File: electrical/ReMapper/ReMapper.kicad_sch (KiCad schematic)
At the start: 50 parts, among them J1 ESP_UART0, J2 I2C Display, J3 USB_IN, J4 USB_OUT, J5 Programming Mode SW, U1 SPX1117M3-L-3-3/TR, U2 W25Q128JVE, U3 ESP32-S3-WROOM-1-N8R8, U4 RP2040, U5 W25Q128JVE, Y1 12MHZ

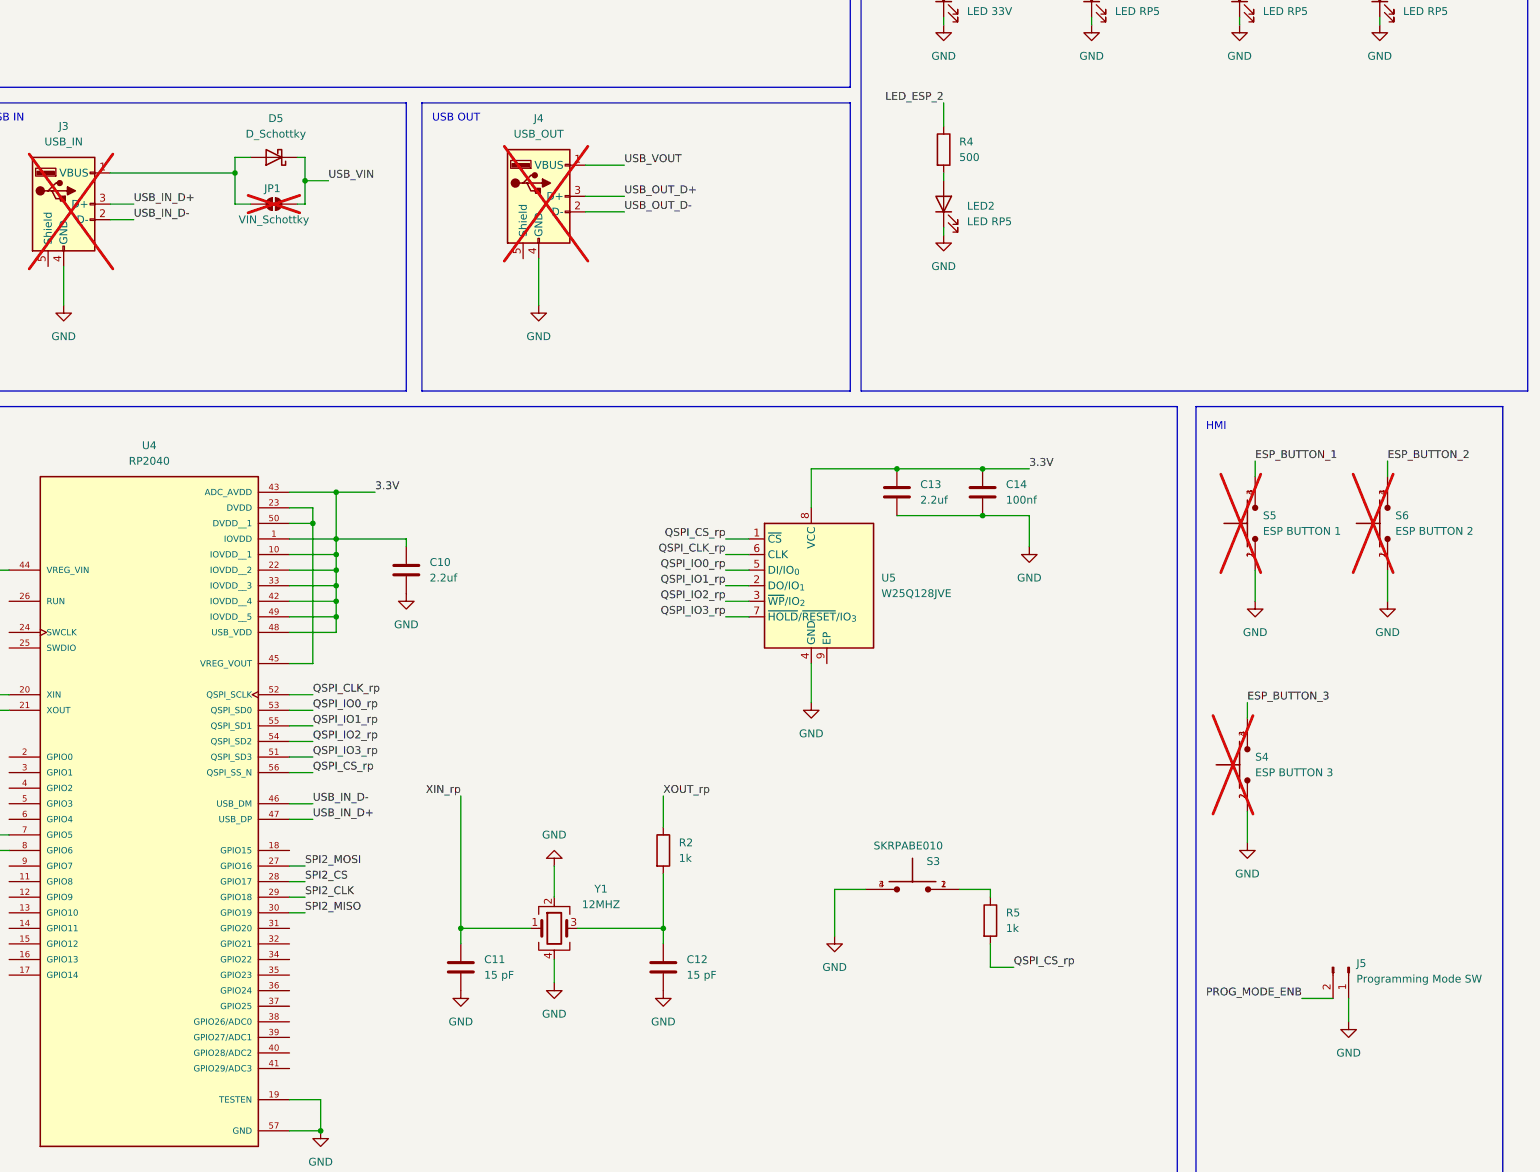
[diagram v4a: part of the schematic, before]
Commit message: more component placement, removed lots of debug and hmi
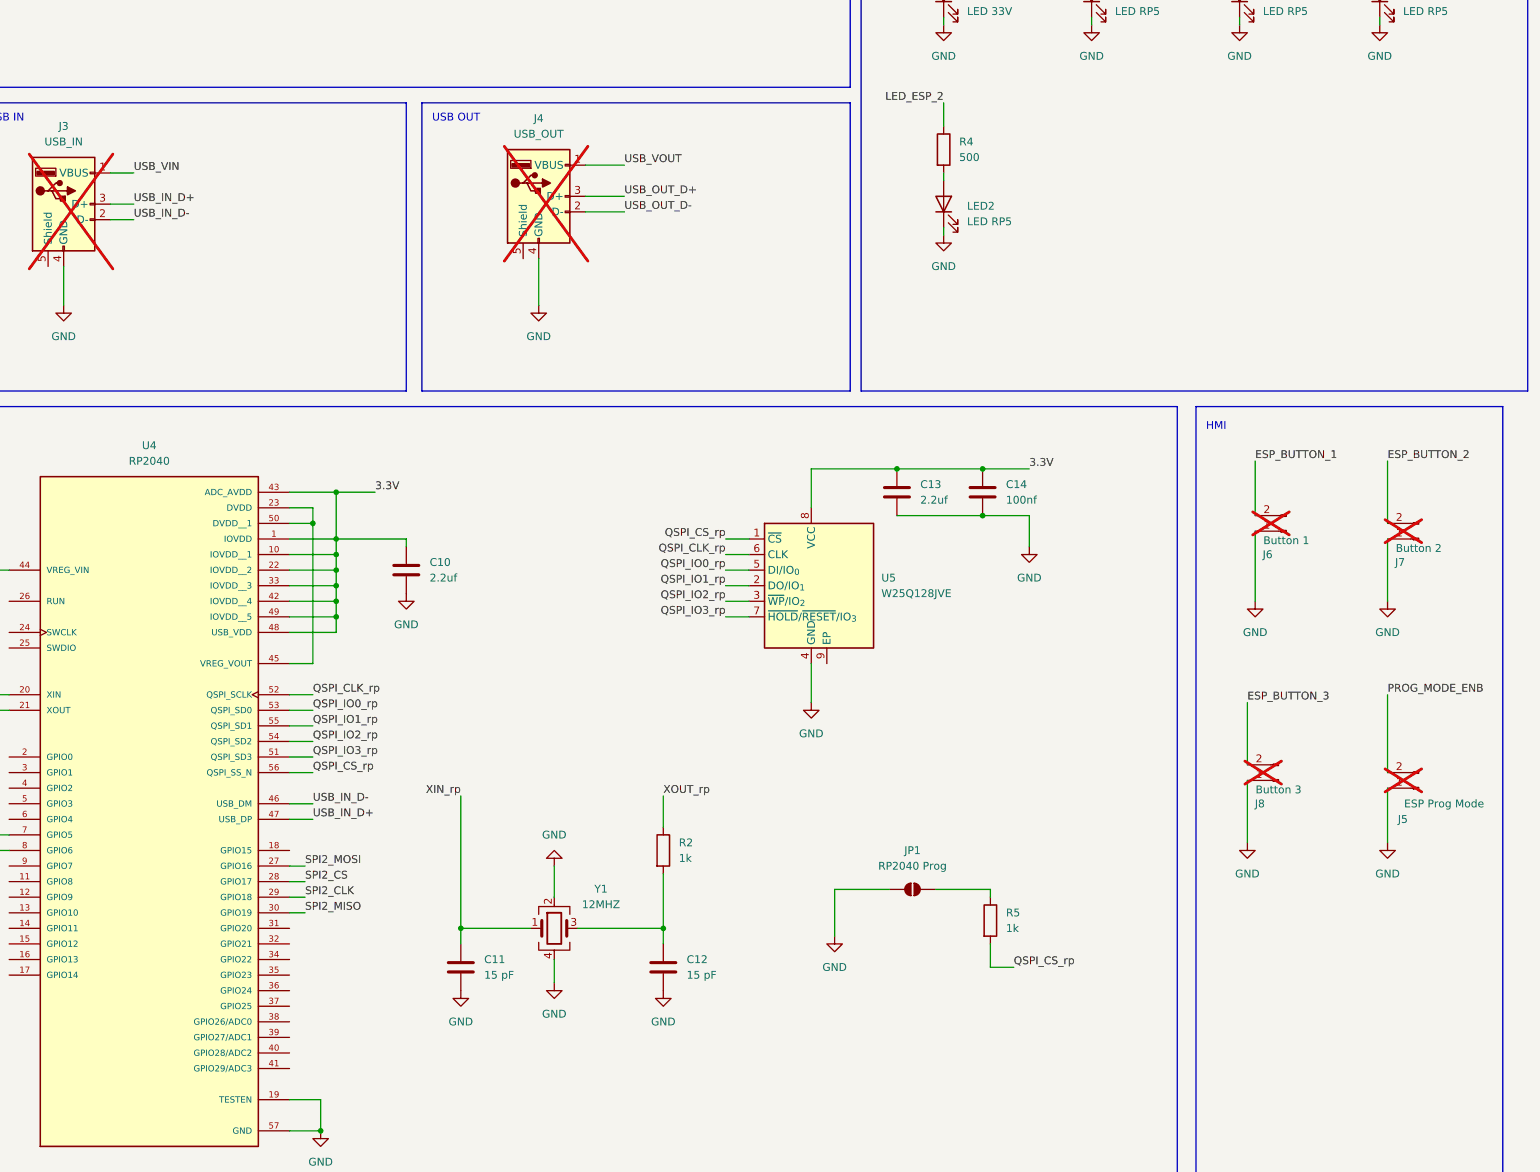
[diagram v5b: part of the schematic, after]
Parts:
- removed D5: D_Schottky, Diode_SMD:D_SOD-123, symbol Device:D_Schottky
- removed S3: SKRPABE010, footprints:push_button_SKRPABE010, symbol push_button_SKRPABE010:SKRPABE010
- removed S4: ESP BUTTON 3, footprints:push_button_SKRPABE010, symbol push_button_SKRPABE010:SKRPABE010
- removed S5: ESP BUTTON 1, footprints:push_button_SKRPABE010, symbol push_button_SKRPABE010:SKRPABE010
- removed S6: ESP BUTTON 2, footprints:push_button_SKRPABE010, symbol push_button_SKRPABE010:SKRPABE010
- added J6: Button 1, Connector_PinHeader_2.54mm:PinHeader_1x02_P2.54mm_Vertical, symbol Connector:Conn_01x02_Pin
- added J7: Button 2, Connector_PinHeader_2.54mm:PinHeader_1x02_P2.54mm_Vertical, symbol Connector:Conn_01x02_Pin
- added J8: Button 3, Connector_PinHeader_2.54mm:PinHeader_1x02_P2.54mm_Vertical, symbol Connector:Conn_01x02_Pin
- J5: value Programming Mode SW -> ESP Prog Mode; now not fitted; now left out of the parts list
- JP1: value VIN_Schottky -> RP2040 Prog; footprint Jumper:SolderJumper-2_P1.3mm_Open_Pad1.0x1.5mm -> Jumper:SolderJumper-2_P1.3mm_Open_RoundedPad1.0x1.5mm; now fitted
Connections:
- net ESP_BUTTON_1: now also J6.2 (Pin_2)
- net ESP_BUTTON_2: now also J7.2 (Pin_2)
- net ESP_BUTTON_3: now also J8.2 (Pin_2)
- net GND: now also JP1.1 (A), J6.1 (Pin_1), J7.1 (Pin_1), J8.1 (Pin_1)
- net USB_VIN: now also J3.1 (VBUS); no longer JP1.2 (B)
- net at R5.1: now also JP1.2 (B)

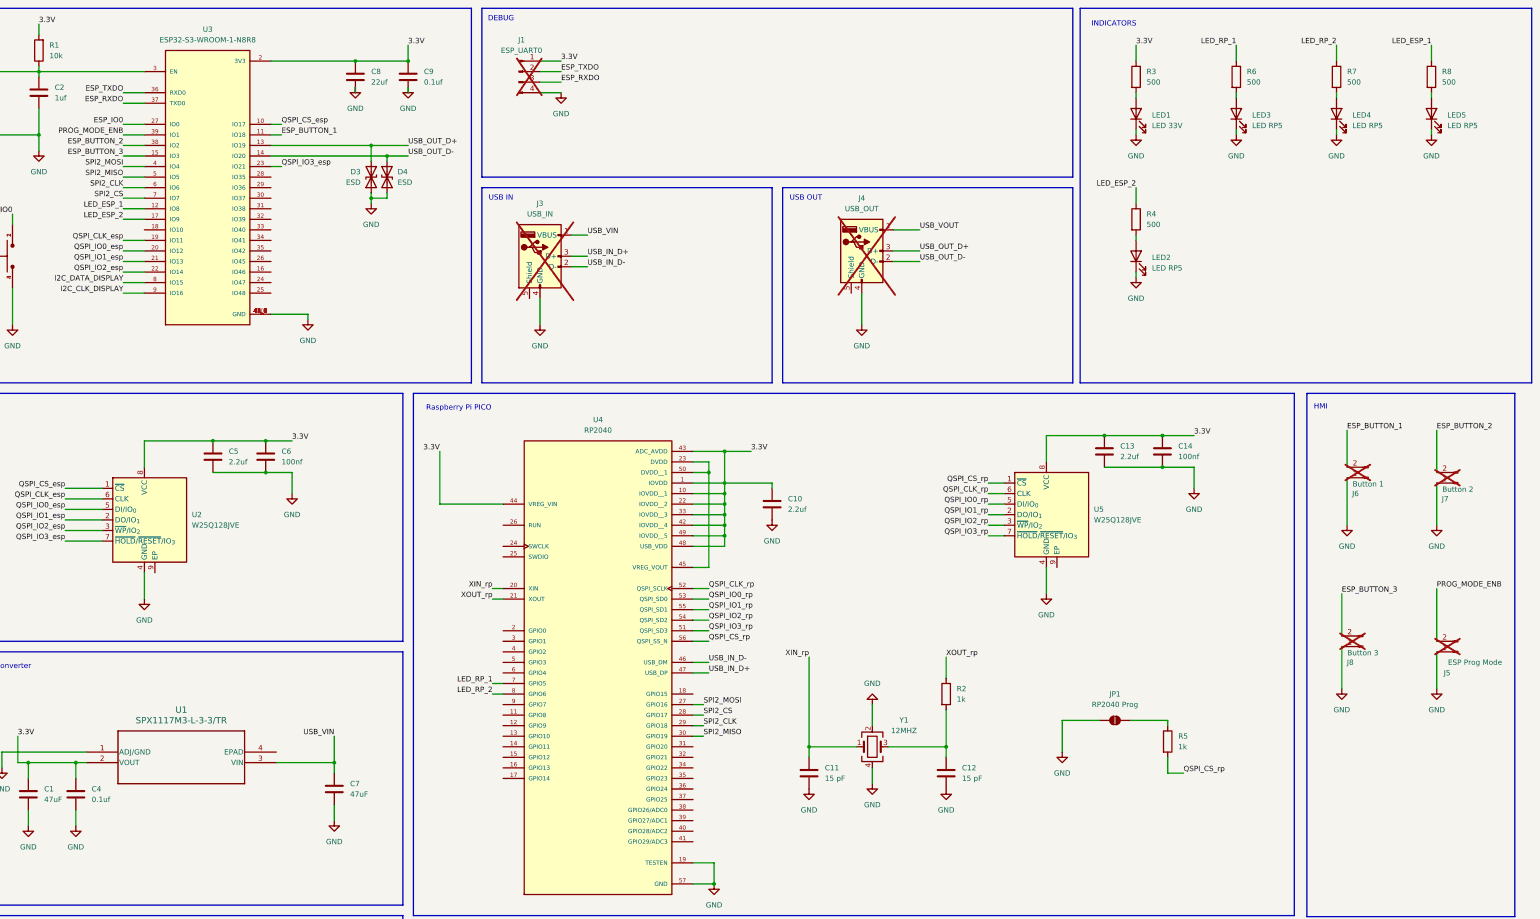
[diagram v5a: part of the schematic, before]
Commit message: first layout attempt, had to compromise on some SMD and shrink the header pins
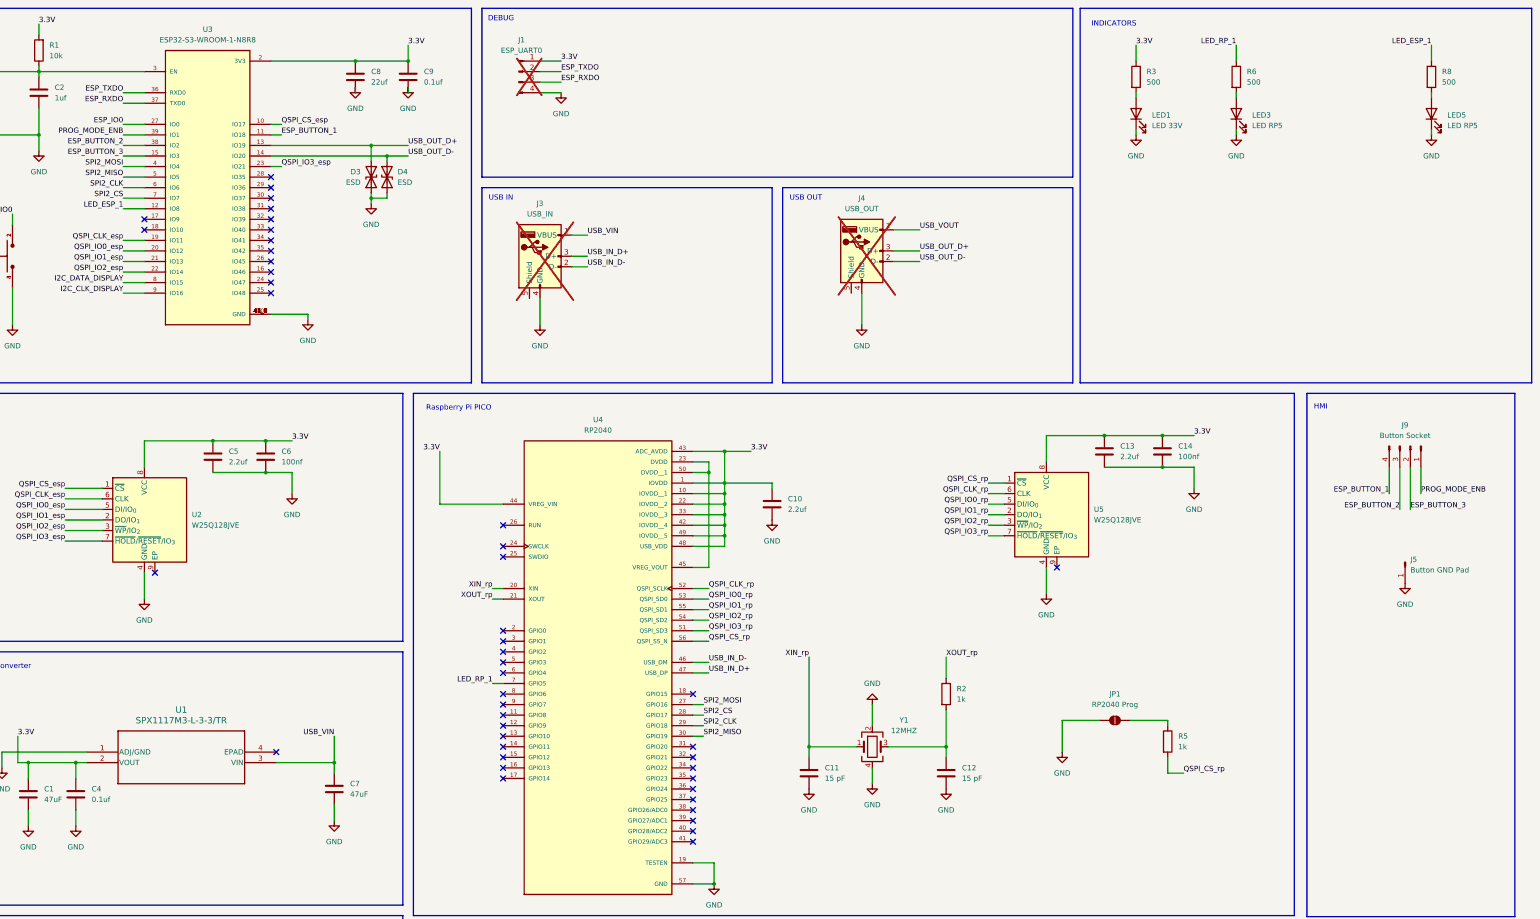
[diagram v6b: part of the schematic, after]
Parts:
- removed J5: ESP Prog Mode, Connector_PinHeader_2.54mm:PinHeader_1x02_P2.54mm_Vertical, symbol Connector:Conn_01x02_Pin
- removed J6: Button 1, Connector_PinHeader_2.54mm:PinHeader_1x02_P2.54mm_Vertical, symbol Connector:Conn_01x02_Pin
- removed J7: Button 2, Connector_PinHeader_2.54mm:PinHeader_1x02_P2.54mm_Vertical, symbol Connector:Conn_01x02_Pin
- removed J8: Button 3, Connector_PinHeader_2.54mm:PinHeader_1x02_P2.54mm_Vertical, symbol Connector:Conn_01x02_Pin
- removed LED2, LED4: LED RP5, LED_SMD:LED_0603_1608Metric, symbol Device:LED
- removed R4, R7: 500, Resistor_SMD:R_0603_1608Metric, symbol Device:R
- added J5: Button GND Pad, TestPoint:TestPoint_Pad_D2.0mm, symbol Connector:Conn_01x01_Pin
- added J9: Button Socket, Connector_PinHeader_1.27mm:PinHeader_1x04_P1.27mm_Vertical_SMD_Pin1Left, symbol Connector:Conn_01x04_Pin
- J1: footprint Connector_PinHeader_2.54mm:PinHeader_1x04_P2.54mm_Vertical -> Connector_PinHeader_1.27mm:PinHeader_1x04_P1.27mm_Vertical_SMD_Pin1Right
- J2: footprint Connector_PinHeader_2.54mm:PinHeader_1x04_P2.54mm_Vertical -> Connector_PinHeader_1.27mm:PinHeader_1x04_P1.27mm_Vertical
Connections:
- net ESP_BUTTON_1: now also J9.4 (Pin_4)
- net ESP_BUTTON_2: now also J9.3 (Pin_3)
- net ESP_BUTTON_3: now also J9.2 (Pin_2)
- net GND: now also J5.1 (Pin_1)
- net PROG_MODE_ENB: now also J9.1 (Pin_1)
- net LED_ESP_2: no longer names the net of U3.17 (IO9)
- net LED_RP_2: no longer names the net of U4.8 (GPIO6)
- no-connect marks 0 -> 45
